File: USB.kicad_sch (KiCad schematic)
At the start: 2 parts, among them IC1 FUSB340TMX, IC2 FUSB340TMX

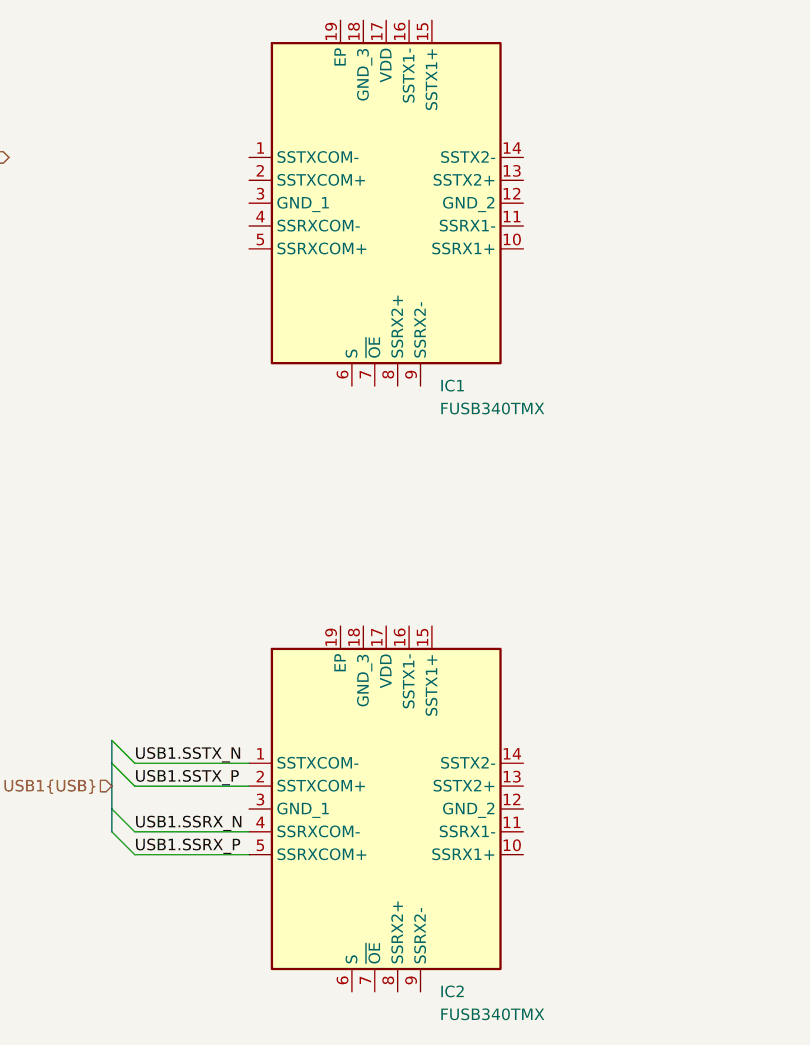
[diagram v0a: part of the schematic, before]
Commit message: USB superspeed muxes
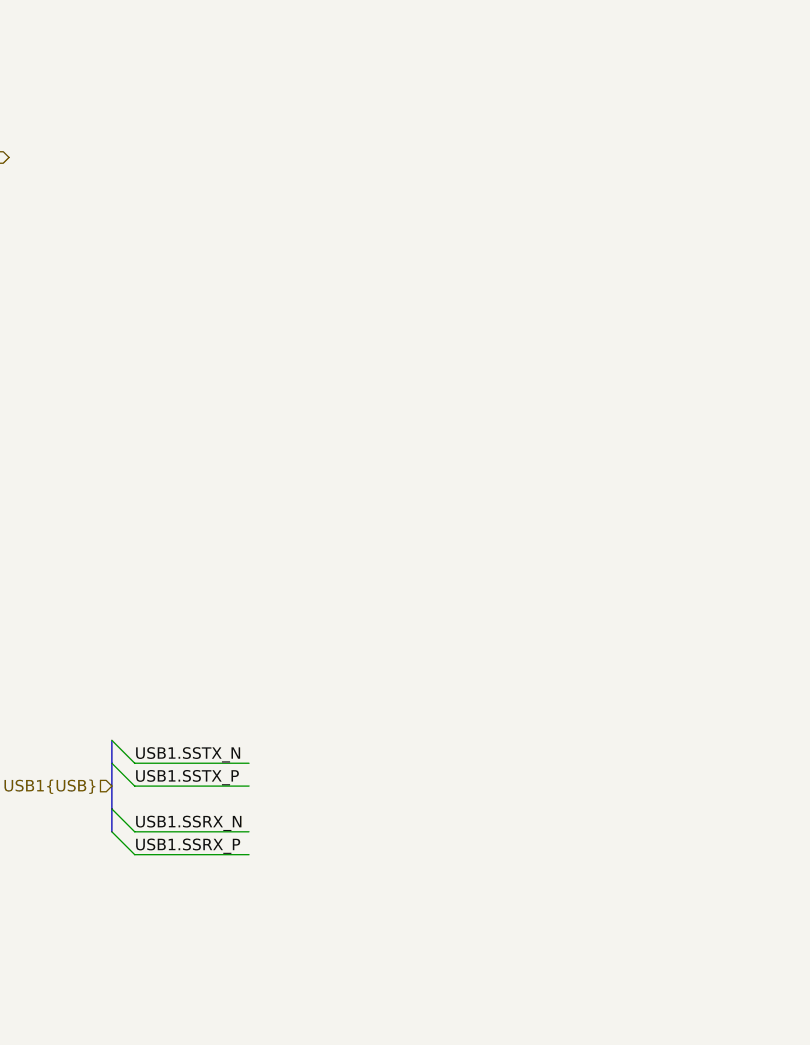
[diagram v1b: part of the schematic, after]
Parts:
- removed IC1, IC2: FUSB340TMX, onsemi:FUSB340TMX, symbol onsemi:FUSB340TMX

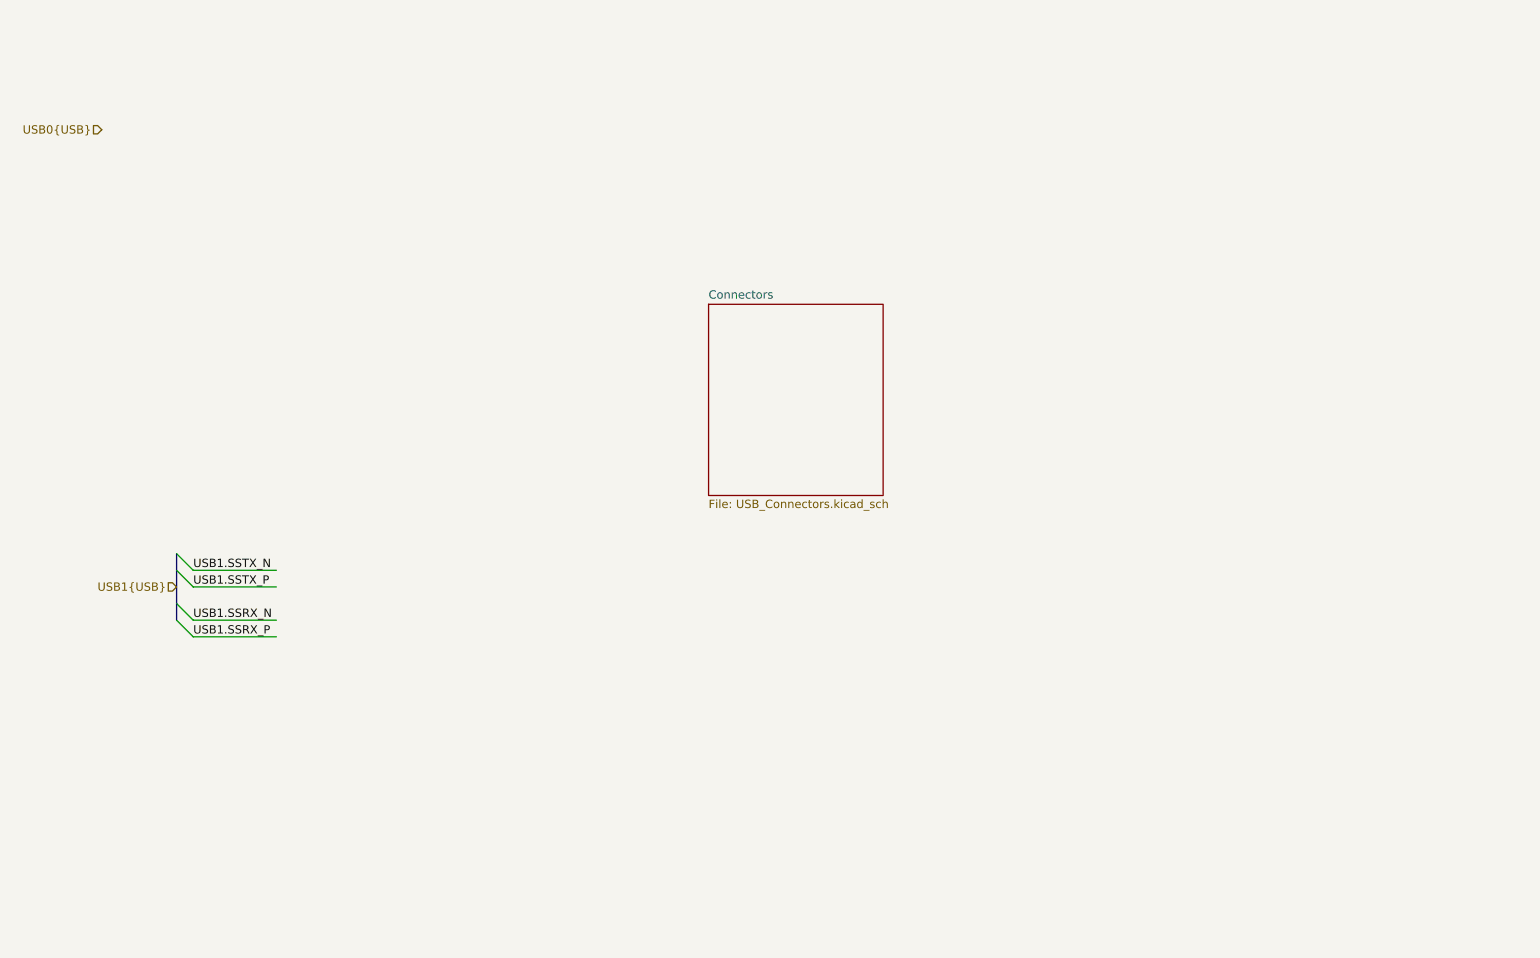
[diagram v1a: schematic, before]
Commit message: USB 2.0 PHY
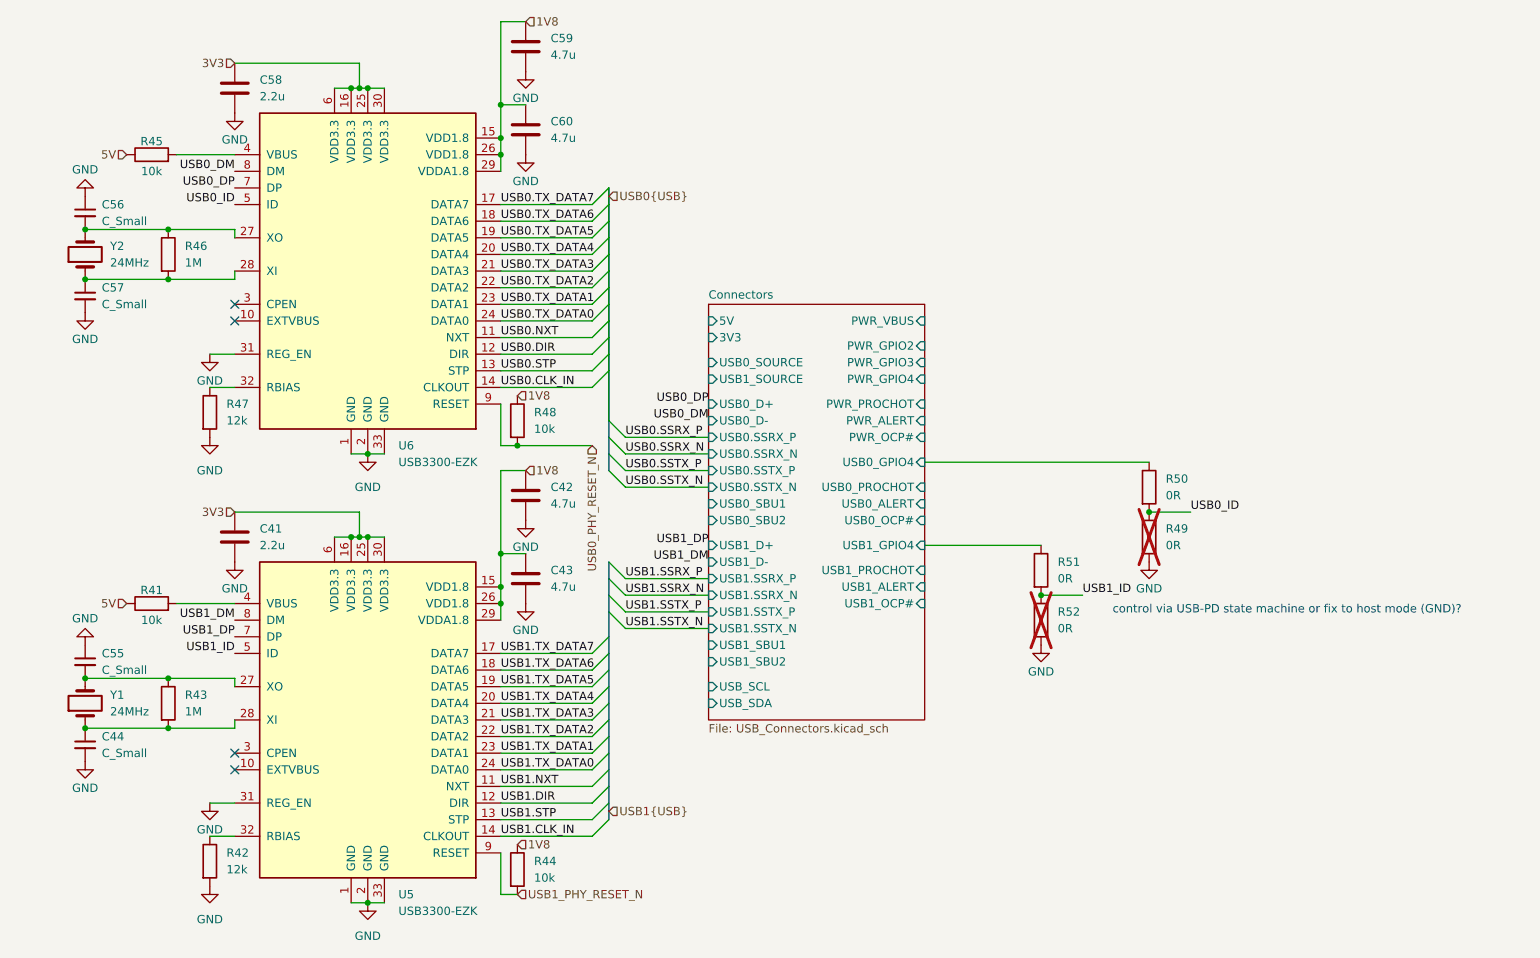
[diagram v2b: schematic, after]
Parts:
- added C41, C58: 2.2u, symbol Device:C
- added C42, C43, C59, C60: 4.7u, symbol Device:C
- added C44, C55, C56, C57: C_Small, symbol Device:C_Small
- added R41, R44, R45, R48: 10k, symbol Device:R
- added R42, R47: 12k, symbol Device:R
- added R43, R46: 1M, symbol Device:R
- added R49, R50, R51, R52: 0R, symbol Device:R
- added U5, U6: USB3300-EZK, Package_DFN_QFN:QFN-32-1EP_5x5mm_P0.5mm_EP3.45x3.45mm, symbol Interface_USB:USB3300-EZK
- added Y1, Y2: 24MHz, symbol Device:Crystal
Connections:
- new net: C44.1, R43.2, U5.28 (XI), Y1.1
- new net: C55.2, R43.1, U5.27 (XO), Y1.2
- new net: R42.1, U5.32 (RBIAS)
- new net: R41.2, U5.4 (VBUS)
- new net: C56.2, R46.1, U6.27 (XO), Y2.2
- new net: C57.1, R46.2, U6.28 (XI), Y2.1
- new net: R45.2, U6.4 (VBUS)
- new net: R47.1, U6.32 (RBIAS)
- new net 1V8: C42.1, C43.1, C59.1, C60.1, R44.1, R48.1, U5.15 (VDD1.8), U5.26 (VDD1.8), U5.29 (VDDA1.8), U6.15 (VDD1.8), U6.26 (VDD1.8), U6.29 (VDDA1.8)
- new net 3V3: C41.1, C58.1, U5.16 (VDD3.3), U5.25 (VDD3.3), U5.30 (VDD3.3), U5.6 (VDD3.3), U6.16 (VDD3.3), U6.25 (VDD3.3), U6.30 (VDD3.3), U6.6 (VDD3.3)
- new net 5V: R41.1, R45.1
- new net Connectors/USB0_GPIO4: R50.1
- new net Connectors/USB1_GPIO4: R51.1
- new net GND: C41.2, C42.2, C43.2, C44.2, C55.1, C56.1, C57.2, C58.2, C59.2, C60.2, R42.2, R47.2, R49.2, R52.2, U5.1 (GND), U5.2 (GND), U5.31 (REG_EN), U5.33 (GND), U6.1 (GND), U6.2 (GND), U6.31 (REG_EN), U6.33 (GND)
- new net USB0.CLK_IN: U6.14 (CLKOUT)
- new net USB0.DIR: U6.12 (DIR)
- new net USB0.NXT: U6.11 (NXT)
- new net USB0.STP: U6.13 (STP)
- new net USB0.TX_DATA0: U6.24 (DATA0)
- new net USB0.TX_DATA1: U6.23 (DATA1)
- new net USB0.TX_DATA2: U6.22 (DATA2)
- new net USB0.TX_DATA3: U6.21 (DATA3)
- new net USB0.TX_DATA4: U6.20 (DATA4)
- new net USB0.TX_DATA5: U6.19 (DATA5)
- new net USB0.TX_DATA6: U6.18 (DATA6)
- new net USB0.TX_DATA7: U6.17 (DATA7)
- new net USB0_DM: U6.8 (DM)
- new net USB0_DP: U6.7 (DP)
- new net USB0_ID: R49.1, R50.2, U6.5 (ID)
- new net USB0_PHY_RESET_N: R48.2, U6.9 (RESET)
- new net USB1.CLK_IN: U5.14 (CLKOUT)
- new net USB1.DIR: U5.12 (DIR)
- new net USB1.NXT: U5.11 (NXT)
- new net USB1.STP: U5.13 (STP)
- new net USB1.TX_DATA0: U5.24 (DATA0)
- new net USB1.TX_DATA1: U5.23 (DATA1)
- new net USB1.TX_DATA2: U5.22 (DATA2)
- new net USB1.TX_DATA3: U5.21 (DATA3)
- new net USB1.TX_DATA4: U5.20 (DATA4)
- new net USB1.TX_DATA5: U5.19 (DATA5)
- new net USB1.TX_DATA6: U5.18 (DATA6)
- new net USB1.TX_DATA7: U5.17 (DATA7)
- new net USB1_DM: U5.8 (DM)
- new net USB1_DP: U5.7 (DP)
- new net USB1_ID: R51.2, R52.1, U5.5 (ID)
- new net USB1_PHY_RESET_N: R44.2, U5.9 (RESET)
- no-connect marks 0 -> 4
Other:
- sheet Connectors ports: added 3V3, 5V, PWR_ALERT, PWR_GPIO2, PWR_GPIO3, PWR_GPIO4, PWR_OCP#, PWR_PROCHOT, PWR_VBUS, USB0.SSRX_N, USB0.SSRX_P, USB0.SSTX_N, USB0.SSTX_P, USB0_ALERT, USB0_D+, USB0_D-, USB0_GPIO4, USB0_OCP#, USB0_PROCHOT, USB0_SBU1, USB0_SBU2, USB0_SOURCE, USB1.SSRX_N, USB1.SSRX_P, USB1.SSTX_N, USB1.SSTX_P, USB1_ALERT, USB1_D+, USB1_D-, USB1_GPIO4, USB1_OCP#, USB1_PROCHOT, USB1_SBU1, USB1_SBU2, USB1_SOURCE, USB_SCL, USB_SDA; removed none
- note added: "control via USB-PD state machine or fix to host mode (GND)?"

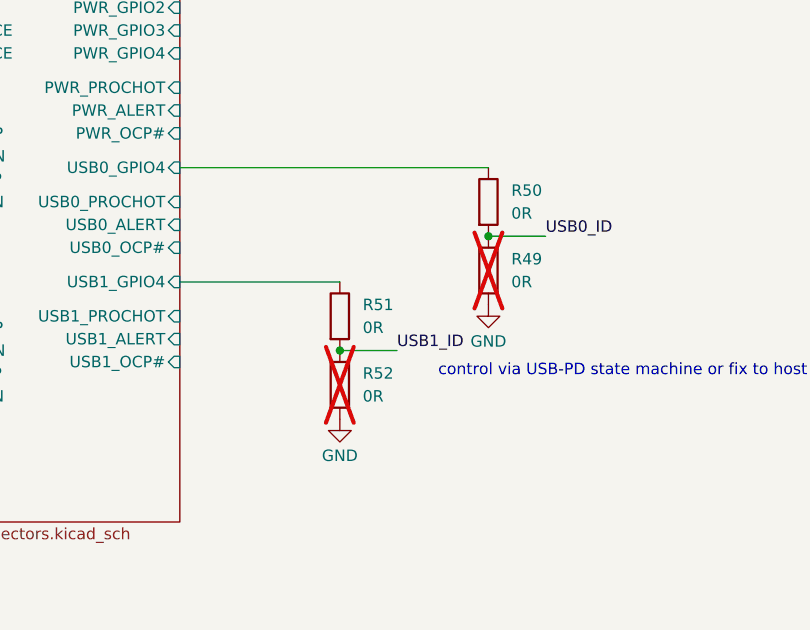
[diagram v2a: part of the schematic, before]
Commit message: fixed ID resistors
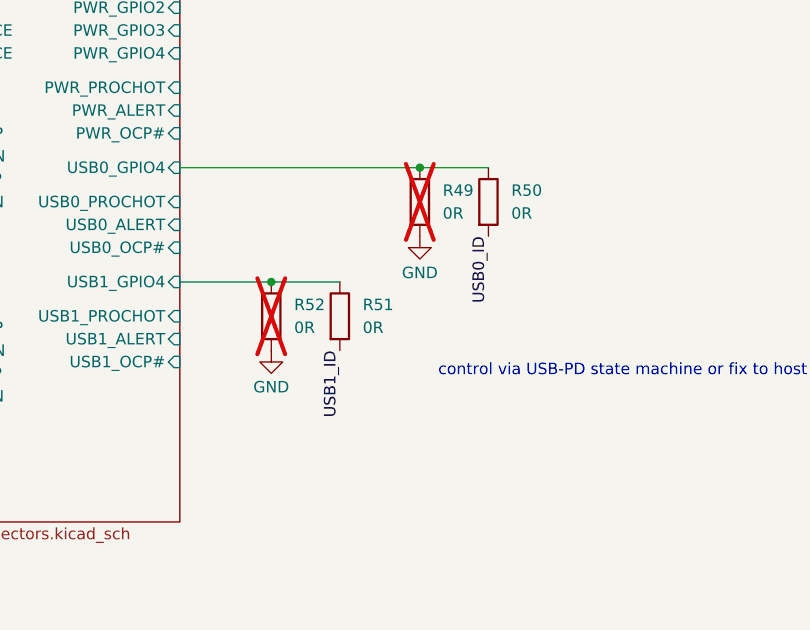
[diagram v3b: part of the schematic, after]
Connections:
- net Connectors/USB0_GPIO4: now also R49.1
- net Connectors/USB1_GPIO4: now also R52.1
- net USB0_ID: no longer R49.1
- net USB1_ID: no longer R52.1
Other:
- moved on the sheet: R49, R52
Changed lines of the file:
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@@
 	)
 	(junction
-		(at 185.42 109.22)
+		(at 177.8 101.6)
 		(diameter 0)
 		(color 0 0 0 0)
@@
 	)
 	(junction
-		(at 168.91 121.92)
+		(at 22.86 66.04)
 		(diameter 0)
 		(color 0 0 0 0)
 	)
 	(junction
-		(at 22.86 66.04)
+		(at 161.29 114.3)
 		(diameter 0)
 		(color 0 0 0 0)
@@
 	(wire
 		(pts
-			(xy 191.77 109.22) (xy 185.42 109.22)
-		)
-		(stroke
-			(width 0)
-			(type default)
-		)
-	)
-	(wire
-		(pts
 			(xy 63.5 113.03) (xy 60.96 113.03)
 		)
@@
 	(wire
 		(pts
-			(xy 151.13 114.3) (xy 168.91 114.3)
+			(xy 151.13 114.3) (xy 161.29 114.3)
 		)
 		(stroke
@@
 	(wire
 		(pts
-			(xy 175.26 121.92) (xy 168.91 121.92)
+			(xy 63.5 100.33) (xy 66.04 100.33)
 		)
 		(stroke
@@
 	(wire
 		(pts
-			(xy 63.5 100.33) (xy 66.04 100.33)
+			(xy 86.36 72.39) (xy 100.33 72.39)
 		)
 		(stroke
@@
 	(wire
 		(pts
-			(xy 86.36 72.39) (xy 100.33 72.39)
+			(xy 66.04 44.45) (xy 68.58 44.45)
 		)
 		(stroke
@@
 		)
 	)
-	(wire
+	(bus
 		(pts
-			(xy 66.04 44.45) (xy 68.58 44.45)
+			(xy 102.87 69.85) (xy 102.87 72.39)
 		)
 		(stroke
@@
 		)
 	)
-	(bus
+	(wire
 		(pts
-			(xy 102.87 69.85) (xy 102.87 72.39)
+			(xy 161.29 114.3) (xy 168.91 114.3)
 		)
 		(stroke
@@
 		)
 	)
+	(wire
+		(pts
+			(xy 177.8 101.6) (xy 185.42 101.6)
+		)
+		(stroke
+			(width 0)
+			(type default)
+		)
+	)
 	(bus
 		(pts
@@
 	(wire
 		(pts
-			(xy 151.13 101.6) (xy 185.42 101.6)
+			(xy 151.13 101.6) (xy 177.8 101.6)
 		)
 		(stroke
@@
 	)
 	(label "USB1_ID"
-		(at 175.26 121.92 0)
+		(at 168.91 121.92 270)
 		(effects
 			(font
 				(size 1.27 1.27)
 			)
-			(justify left bottom)
+			(justify right bottom)
 		)
 	)
@@
 	)
 	(label "USB0_ID"
-		(at 191.77 109.22 0)
+		(at 185.42 109.22 270)
 		(effects
 			(font
 				(size 1.27 1.27)
 			)
-			(justify left bottom)
+			(justify right bottom)
 		)
 	)
@@
 	(symbol
 		(lib_id "Device:R")
-		(at 185.42 113.03 0)
+		(at 177.8 105.41 0)
 		(unit 1)
 		(exclude_from_sim no)
@@
 		(fields_autoplaced yes)
 		(property "Reference" "R49"
-			(at 187.96 111.7599 0)
+			(at 180.34 104.1399 0)
 			(effects
 				(font
@@
 		)
 		(property "Value" "0R"
-			(at 187.96 114.2999 0)
+			(at 180.34 106.6799 0)
 			(effects
 				(font
@@
 		)
 		(property "Footprint" ""
-			(at 183.642 113.03 90)
+			(at 176.022 105.41 90)
 			(effects
 				(font
@@
 		)
 		(property "Datasheet" "~"
-			(at 185.42 113.03 0)
+			(at 177.8 105.41 0)
 			(effects
 				(font
@@
 		)
 		(property "Description" "Resistor"
-			(at 185.42 113.03 0)
+			(at 177.8 105.41 0)
 			(effects
 				(font
@@
 	(symbol
 		(lib_id "Device:R")
-		(at 168.91 125.73 0)
+		(at 161.29 118.11 0)
 		(unit 1)
 		(exclude_from_sim no)
@@
 		(fields_autoplaced yes)
 		(property "Reference" "R52"
-			(at 171.45 124.4599 0)
+			(at 163.83 116.8399 0)
 			(effects
 				(font
@@
 		)
 		(property "Value" "0R"
-			(at 171.45 126.9999 0)
+			(at 163.83 119.3799 0)
 			(effects
 				(font
@@
 		)
 		(property "Footprint" ""
-			(at 167.132 125.73 90)
+			(at 159.512 118.11 90)
 			(effects
 				(font
@@
 		)
 		(property "Datasheet" "~"
-			(at 168.91 125.73 0)
+			(at 161.29 118.11 0)
 			(effects
 				(font
@@
 		)
 		(property "Description" "Resistor"
-			(at 168.91 125.73 0)
+			(at 161.29 118.11 0)
 			(effects
 				(font
@@
 	(symbol
 		(lib_id "power:GND")
-		(at 185.42 116.84 0)
+		(at 177.8 109.22 0)
 		(unit 1)
 		(exclude_from_sim no)
@@
 		(dnp no)
 		(property "Reference" "#PWR086"
-			(at 185.42 123.19 0)
+			(at 177.8 115.57 0)
 			(effects
 				(font
@@
 		)
 		(property "Value" "GND"
-			(at 185.42 120.904 0)
+			(at 177.8 113.284 0)
 			(effects
 				(font
@@
 		)
 		(property "Footprint" ""
-			(at 185.42 116.84 0)
+			(at 177.8 109.22 0)
 			(effects
 				(font
@@
 		)
 		(property "Datasheet" ""
-			(at 185.42 116.84 0)
+			(at 177.8 109.22 0)
 			(effects
 				(font
@@
 		)
 		(property "Description" "Power symbol creates a global label with name \"GND\" , ground"
-			(at 185.42 116.84 0)
+			(at 177.8 109.22 0)
 			(effects
 				(font
@@
 	(symbol
 		(lib_id "power:GND")
-		(at 168.91 129.54 0)
+		(at 161.29 121.92 0)
 		(unit 1)
 		(exclude_from_sim no)
@@
 		(dnp no)
 		(property "Reference" "#PWR081"
-			(at 168.91 135.89 0)
+			(at 161.29 128.27 0)
 			(effects
 				(font
@@
 		)
 		(property "Value" "GND"
-			(at 168.91 133.604 0)
+			(at 161.29 125.984 0)
 			(effects
 				(font
@@
 		)
 		(property "Footprint" ""
-			(at 168.91 129.54 0)
+			(at 161.29 121.92 0)
 			(effects
 				(font
@@
 		)
 		(property "Datasheet" ""
-			(at 168.91 129.54 0)
+			(at 161.29 121.92 0)
 			(effects
 				(font
@@
 		)
 		(property "Description" "Power symbol creates a global label with name \"GND\" , ground"
-			(at 168.91 129.54 0)
+			(at 161.29 121.92 0)
 			(effects
 				(font
